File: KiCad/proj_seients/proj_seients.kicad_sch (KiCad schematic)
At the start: 37 parts, among them J1 BATERIA 12V, J2 Hebilla comercial con sensor 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, J3 Conexiones al Bus del Coche, J4 Motor, J5 Motor, J6 Motor, U1 PIC24HJ128GP502, U2 LM2596S-5, U3 LM1117DT-3.3, U4 TCAN1043xDxQ1, U5 PCA9685BS, U6 DRV8871DDA, U7 DRV8871DDA, U8 DRV8871DDA, Y1 Crystal

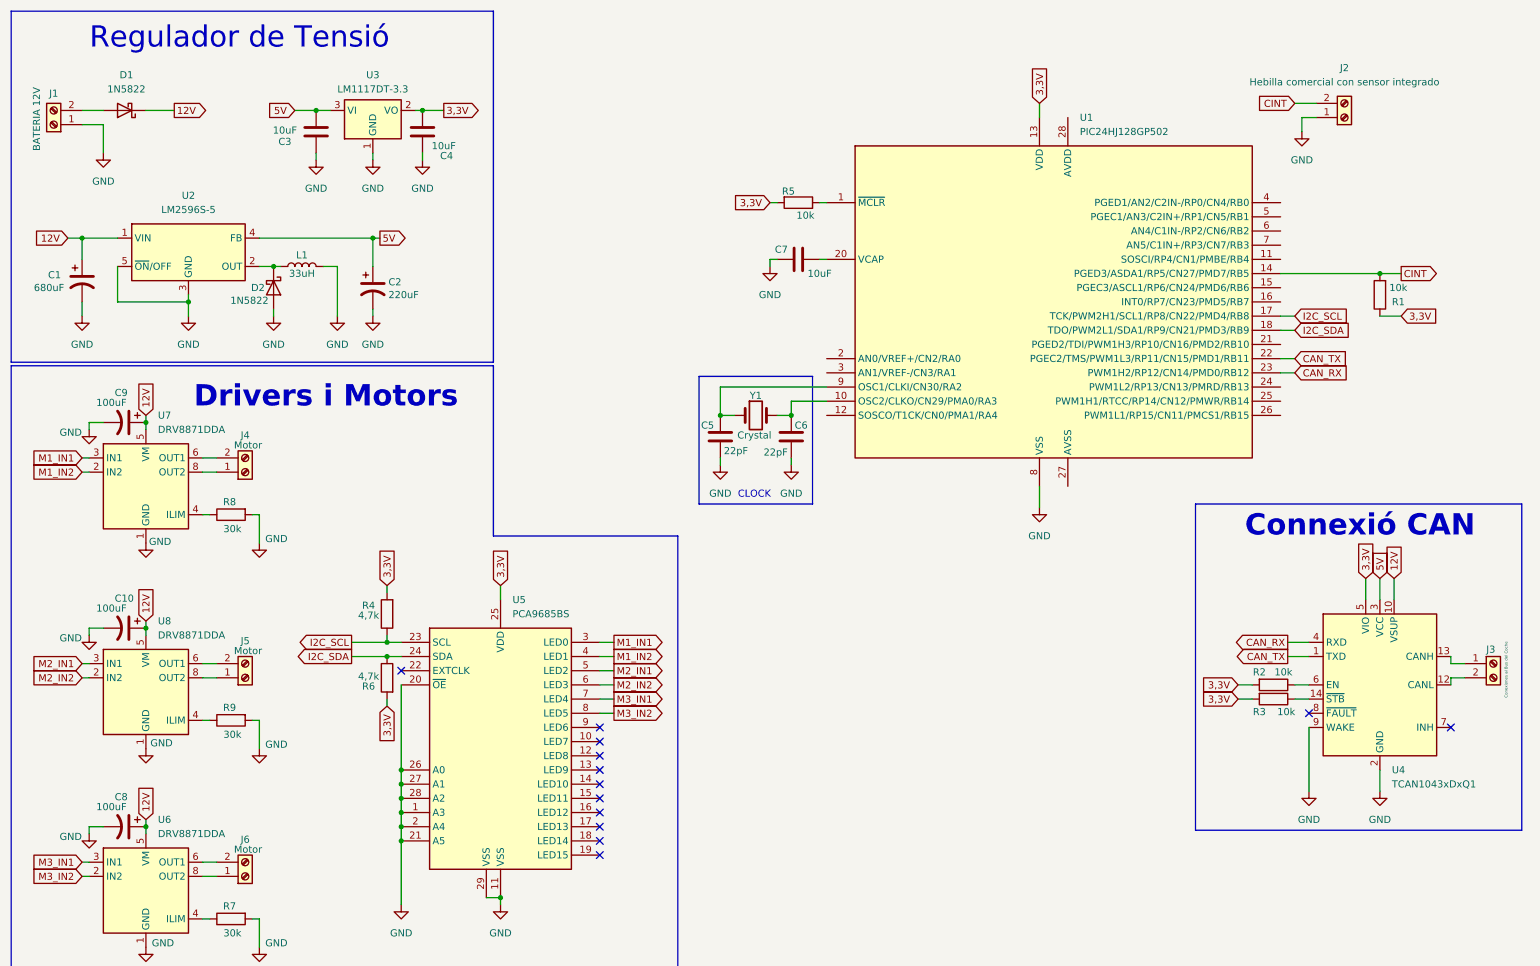
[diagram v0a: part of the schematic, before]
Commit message: Afegit calefacor + alguns LEDs
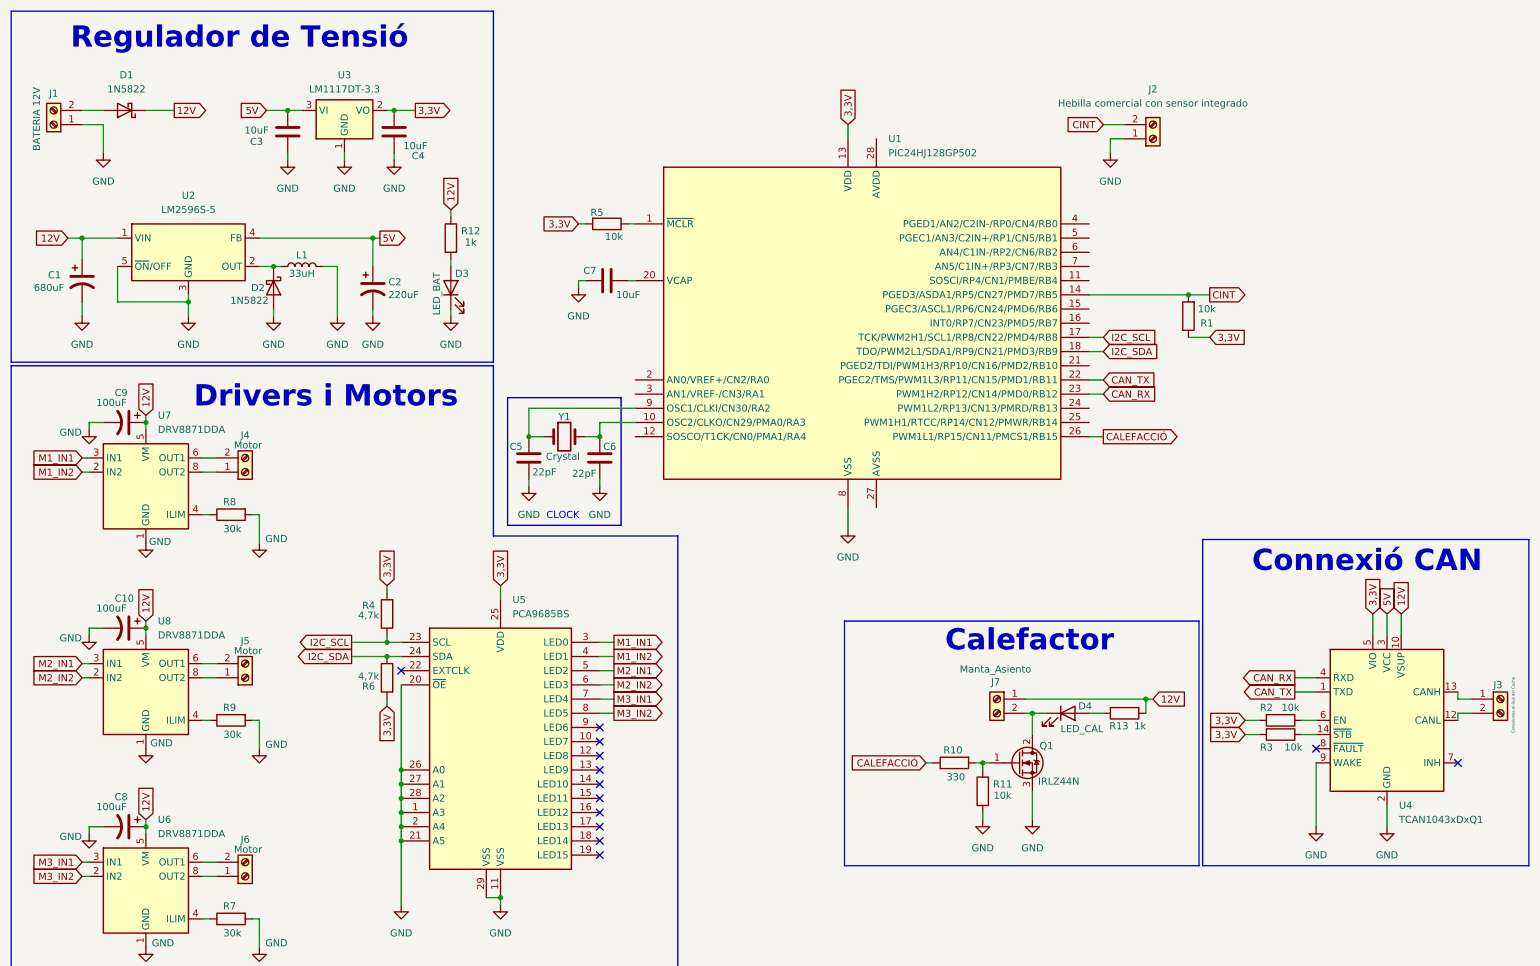
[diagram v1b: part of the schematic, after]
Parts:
- added D3: LED_BAT, symbol Device:LED
- added D4: LED_CAL, symbol Device:LED
- added J7: Manta_Asiento, symbol Connector:Screw_Terminal_01x02
- added Q1: IRLZ44N, Package_TO_SOT_THT:TO-220-3_Vertical, symbol Transistor_FET:IRLZ44N
- added R10: 330, symbol Device:R
- added R11: 10k, symbol Device:R
- added R12, R13: 1k, symbol Device:R
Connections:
- net 12V: now also J7.1 (Pin_1), R12.1, R13.2
- net GND: now also D3.1 (K), Q1.3 (S), R11.2
- net CALEFACCIÓ: now reaches U1.26 (PWM1L1/RP15/CN11/PMCS1/RB15)
- net CALEFACCIÓ: now also R10.1
- new net: D4.2 (A), R13.1
- new net: Q1.1 (G), R10.2, R11.1
- new net: D4.1 (K), J7.2 (Pin_2), Q1.2 (D)
- new net: D3.2 (A), R12.2
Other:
- note added: "Calefactor"
- moved on the sheet: C3, C4, C5, C6, C7, J2, J3, R1, R2, R3, R5, U1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

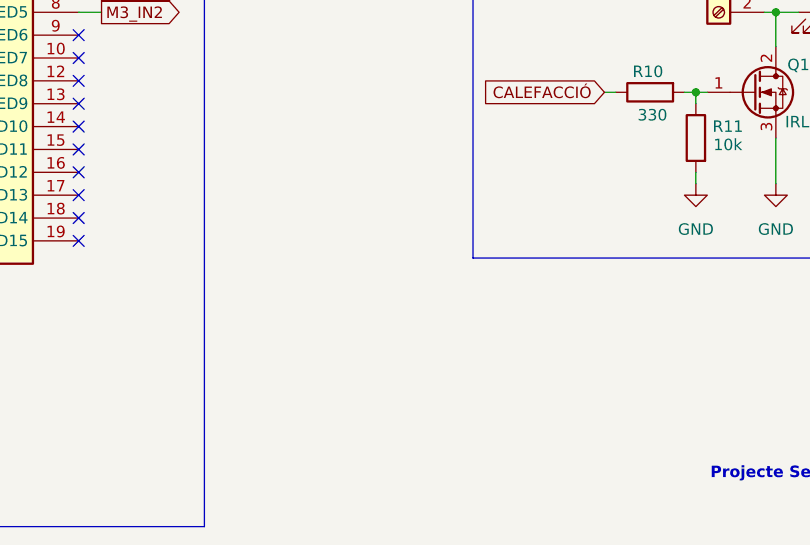
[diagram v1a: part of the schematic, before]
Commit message: Afegit EEPROM
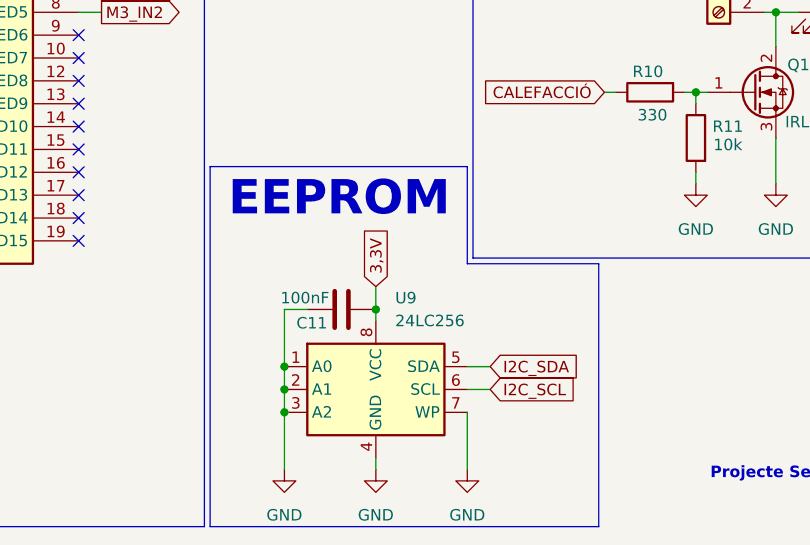
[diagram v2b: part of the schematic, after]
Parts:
- added C11: 100nF, symbol Device:C
- added U9: 24LC256, symbol Memory_EEPROM:24LC256
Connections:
- net 3,3V: now also C11.1, U9.8 (VCC)
- net GND: now also C11.2, U9.1 (A0), U9.2 (A1), U9.3 (A2), U9.4 (GND), U9.7 (WP)
- net I2C_SCL: now also U9.6 (SCL)
- net I2C_SDA: now also U9.5 (SDA)
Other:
- note added: "EEPROM"

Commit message: Afegit MAX3232
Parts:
- added C12, C13, C14, C15: 100nF, symbol Device:C
- added J8: DE9_Socket, Connector_Dsub:DSUB-9_Socket_Vertical_P2.77x2.84mm, symbol Connector:DE9_Socket
- added U10: MAX3232, symbol Interface_UART:MAX3232
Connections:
- net 3,3V: now also C14.1, U10.16 (VCC)
- net GND: now also C15.1, J8.5, U10.15 (GND)
- net UART_TX: now reaches U1.6 (AN4/C1IN-/RP2/CN6/RB2)
- net UART_TX: now also U10.11 (T1IN)
- net UART_RX: now reaches U1.7 (AN5/C1IN+/RP3/CN7/RB3)
- net UART_RX: now also U10.12 (R1OUT)
- new net: C13.1, U10.5 (C2-)
- new net: C13.2, U10.4 (C2+)
- new net: C12.2, U10.1 (C1+)
- new net: C14.2, U10.2 (VS+)
- new net: C12.1, U10.3 (C1-)
- new net: C15.2, U10.6 (VS-)
- new net R1IN: J8.3, U10.13 (R1IN)
- new net T1OUT: J8.2, U10.14 (T1OUT)
- no-connect marks 13 -> 23
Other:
- note added: "17/03/2026"
- note added: "Conector DE-9"
- moved on the sheet: J2, R1

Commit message: Tot Afegit
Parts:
- added C16, C17, C18, C19, C20, C21, C22, C23, C24: 100nF, symbol Device:C
- added J10: Screw_Terminal_01x05, symbol Connector:Screw_Terminal_01x05
- added J11, J12, J13, J14, J15, J16, J17, J18, J9: PushButton, symbol Connector:Screw_Terminal_01x02
- added R14, R15, R16, R17, R18, R19, R20, R21, R22: 10k, symbol Device:R
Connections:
- net 3,3V: now also J10.2 (Pin_2), R14.2, R15.2, R16.2, R17.2, R18.2, R19.2, R20.2, R21.2, R22.2
- net GND: now also C16.1, C17.1, C18.1, C19.1, C20.1, C21.1, C22.1, C23.1, C24.1, J10.3 (Pin_3), J11.1 (Pin_1), J12.1 (Pin_1), J13.1 (Pin_1), J14.1 (Pin_1), J15.1 (Pin_1), J16.1 (Pin_1), J17.1 (Pin_1), J18.1 (Pin_1), J9.1 (Pin_1)
- net at R5.1, U1.1 (~{MCLR}): now also J10.1 (Pin_1)
- net BTN_SUBIR: now reaches U1.11 (SOSCI/RP4/CN1/PMBE/RB4)
- net BTN_SUBIR: now also C19.2, J13.2 (Pin_2), R17.1
- net BTN_ATRAS: now reaches U1.12 (SOSCO/T1CK/CN0/PMA1/RA4)
- net BTN_ATRAS: now also C18.2, J12.2 (Pin_2), R16.1
- net BTN_RECLINAR: now reaches U1.15 (PGEC3/ASCL1/RP6/CN24/PMD6/RB6)
- net BTN_RECLINAR: now also C24.2, J18.2 (Pin_2), R22.1
- net BTN_RECTO: now reaches U1.16 (INT0/RP7/CN23/PMD5/RB7)
- net BTN_RECTO: now also C22.2, J16.2 (Pin_2), R20.1
- net BTN_ADELANTE: now reaches U1.2 (AN0/VREF+/CN2/RA0)
- net BTN_ADELANTE: now also C21.2, J15.2 (Pin_2), R19.1
- net LIM_POSICION: now reaches U1.21 (PGED2/TDI/PWM1H3/RP10/CN16/PMD2/RB10)
- net LIM_POSICION: now also C23.2, J17.2 (Pin_2), R21.1
- net LIM_RECLINACION: now reaches U1.25 (PWM1H1/RTCC/RP14/CN12/PMWR/RB14)
- net LIM_RECLINACION: now also C16.2, J9.2 (Pin_2), R14.1
- net BTN_BAJAR: now reaches U1.3 (AN1/VREF-/CN3/RA1)
- net BTN_BAJAR: now also C20.2, J14.2 (Pin_2), R18.1
- net PGED1: now reaches U1.4 (PGED1/AN2/C2IN-/RP0/CN4/RB0)
- net PGED1: now also J10.4 (Pin_4)
- net PGEC1: now reaches U1.5 (PGEC1/AN3/C2IN+/RP1/CN5/RB1)
- net PGEC1: now also J10.5 (Pin_5)
- new net LIM_ALTURA: C17.2, J11.2 (Pin_2), R15.1
- no-connect marks 23 -> 26
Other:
- moved on the sheet: J2, J8, R1, R4, R6, U5

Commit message: Canvi Connexió AVDD i AVSS
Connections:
- net 3,3V: now also U1.28 (AVDD)
- net GND: now also U1.27 (AVSS)
- no-connect marks 26 -> 24
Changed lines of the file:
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@@
+	)
+	(junction
+		(at 162.56 101.6)
+		(diameter 0)
+		(color 0 0 0 0)
 	)
 	(junction
@@
 	)
 	(no_connect
-		(at 167.64 101.6)
-	)
-	(no_connect
 		(at 102.87 143.51)
 	)
 	(no_connect
-		(at 167.64 35.56)
-	)
-	(no_connect
 		(at 102.87 138.43)
 	)
@@
 		)
 	)
+	(wire
+		(pts
+			(xy 162.56 35.56) (xy 167.64 35.56)
+		)
+		(stroke
+			(width 0)
+			(type default)
+		)
+	)
 	(polyline
 		(pts
@@
 		)
 		(stroke
+			(width 0)
+			(type default)
+		)
+	)
+	(wire
+		(pts
+			(xy 162.56 101.6) (xy 167.64 101.6)
+		)
+		(stroke

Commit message: Correcions proposades
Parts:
- removed C1: 680uF, symbol Device:C_Polarized_US
- removed C10, C8, C9: 100uF, symbol Device:C_Polarized_US
- removed C2: 220uF, symbol Device:C_Polarized_US
- removed C3, C4: 10uF, symbol Device:C
- removed D1, D2: 1N5822, Diode_THT:D_DO-201AD_P15.24mm_Horizontal, symbol Diode:1N5822
- removed D3: LED_BAT, symbol Device:LED
- removed D4: LED_CAL, symbol Device:LED
- removed J1: BATERIA 12V, symbol Connector:Screw_Terminal_01x02
- removed J4, J5, J6: Motor, symbol Connector:Screw_Terminal_01x02
- removed J7: Manta_Asiento, symbol Connector:Screw_Terminal_01x02
- removed L1: 33uH, symbol Device:L
- removed Q1: IRLZ44N, Package_TO_SOT_THT:TO-220-3_Vertical, symbol Transistor_FET:IRLZ44N
- removed R10: 330, symbol Device:R
- removed R11: 10k, symbol Device:R
- removed R12, R13: 1k, symbol Device:R
- removed R4, R6: 4,7k, symbol Device:R
- removed R7, R8, R9: 30k, symbol Device:R
- removed U2: LM2596S-5, Package_TO_SOT_SMD:TO-263-5_TabPin3, symbol Regulator_Switching:LM2596S-5
- removed U3: LM1117DT-3.3, Package_TO_SOT_SMD:TO-252-3_TabPin2, symbol Regulator_Linear:LM1117DT-3.3
- removed U5: PCA9685BS, Package_DFN_QFN:QFN-28-1EP_6x6mm_P0.65mm_EP4.25x4.25mm, symbol Driver_LED:PCA9685BS
- removed U6, U7, U8: DRV8871DDA, Package_SO:Texas_HTSOP-8-1EP_3.9x4.9mm_P1.27mm_EP2.95x4.9mm_Mask2.4x3.1mm_ThermalVias, symbol Driver_Motor:DRV8871DDA
- added C25, C26, C27, C30, C31, C32, C33, C34: 100nF, symbol Device:C
- added C28: 10uF, symbol Device:C_Polarized_US
- added SW1: SW_Push, symbol Switch:SW_Push
- J2: value Hebilla comercial con sensor integrado -> 5f0857756ylz
- J3: value Conexiones al Bus del Coche -> DE-9
- Y1: value Crystal -> 8MHz
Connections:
- net 12V: now also C26.2
- net 5V: now also C27.2, C28.1
- net GND: now also C25.1, C26.1, C27.1, C28.2, C30.1, C31.1, C32.1, C33.1, C34.1, SW1.1; no longer U1.19 (VSS), U1.27 (AVSS), U1.8 (VSS)
- net at J10.1 (Pin_1), R5.1, U1.1 (~{MCLR}): now also SW1.2
- net 3,3V renamed 3.3V
- net 3.3V: now also C25.2, C30.2, C31.2, C32.2
- net R1IN renamed RX
- net T1OUT renamed TX
- new net: C33.2, C34.2, U1.19 (VSS), U1.27 (AVSS), U1.8 (VSS)
- no-connect marks 24 -> 13
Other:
- added sheet Potencia (untitled.kicad_sch)
- note added: "Autors: Miguel Tovar i Pol Salas"
- note added: "Hebilla comercial con sensor integrado"
- note added: "MAX3232"
- note added: "MICROCONTROLADOR"
- note added: "Placa de Control - Seients Elèctrics"
- note added: "Pulsadors i finals de carrera"
- note added: "v1.0"
- note removed: "Calefactor"
- note removed: "Drivers i Motors"
- note removed: "Projecte Seients - Miguel Tovar i Pol Salas"
- note removed: "Regulador de Tensió"
- moved on the sheet: C11, C12, C13, C14, C15, C16, C17, C18, C19, C20, C21, C22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

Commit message: Canvis visuals
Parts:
- removed C11, C12, C13, C14, C15, C16, C17, C18, C19, C20, C21, C22, C23, C24, C25, C26, C27, C30, C31, C32, C33, C34: 100nF, symbol Device:C
- removed C28: 10uF, symbol Device:C_Polarized_US
- removed C5, C6: 22pF, symbol Device:C
- removed C7: 10uF, symbol Device:C
- removed J10: Screw_Terminal_01x05, symbol Connector:Screw_Terminal_01x05
- removed J11, J12, J13, J14, J15, J16, J17, J18, J9: PushButton, symbol Connector:Screw_Terminal_01x02
- removed J2: 5f0857756ylz, symbol Connector:Screw_Terminal_01x02
- removed J3: DE-9, symbol Connector:Screw_Terminal_01x02
- removed J8: DE9_Socket, Connector_Dsub:DSUB-9_Socket_Vertical_P2.77x2.84mm, symbol Connector:DE9_Socket
- removed R1, R14, R15, R16, R17, R18, R19, R2, R20, R21, R22, R3, R5: 10k, symbol Device:R
- removed SW1: SW_Push, symbol Switch:SW_Push
- removed U1: PIC24HJ128GP502, Package_SO:SOIC-28W_7.5x17.9mm_P1.27mm, symbol DSP_Microchip_DSPIC33:DSPIC33FJ64MC802-xSP
- removed U10: MAX3232, symbol Interface_UART:MAX3232
- removed U4: TCAN1043xDxQ1, Package_SO:SOIC-14_3.9x8.7mm_P1.27mm, symbol Interface_CAN_LIN:TCAN1043xDxQ1
- removed U9: 24LC256, symbol Memory_EEPROM:24LC256
- removed Y1: 8MHz, symbol Device:Crystal
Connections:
- no-connect marks 13 -> 0
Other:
- removed sheet Potencia
- added sheet micro i extra (microiextra.kicad_sch)
- added sheet potencia (potencia.kicad_sch)
- note removed: "CLOCK"
- note removed: "Conector DE-9"
- note removed: "Connexió CAN"
- note removed: "EEPROM"
- note removed: "Hebilla comercial con sensor integrado"
- note removed: "MAX3232"
- note removed: "MICROCONTROLADOR"
- note removed: "Pulsadors i finals de carrera"
